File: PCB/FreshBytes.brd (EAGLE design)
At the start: 180.3 x 73.3 mm, 30 parts, among them T1 2N2222, T2 2N2222, T3 2N2222, T4 2N2222, X1 22-23-2021

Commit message: Add logo to BRD file, create gerbers, update BOM
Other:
- board size 180.3 x 73.3 mm -> 181 x 74 mm

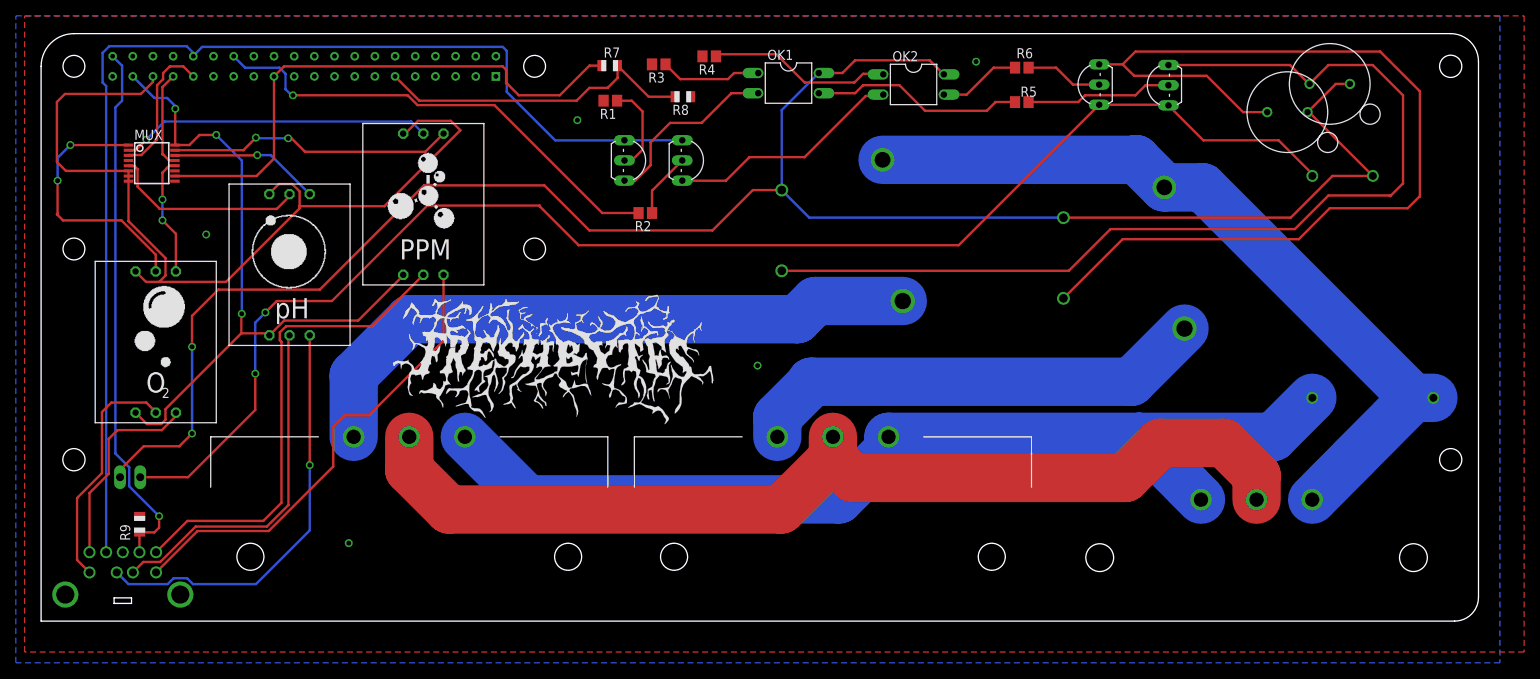
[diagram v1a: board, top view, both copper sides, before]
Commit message: Fix drill size for RPi headers. Swapping over to Rhino for CAD stuff
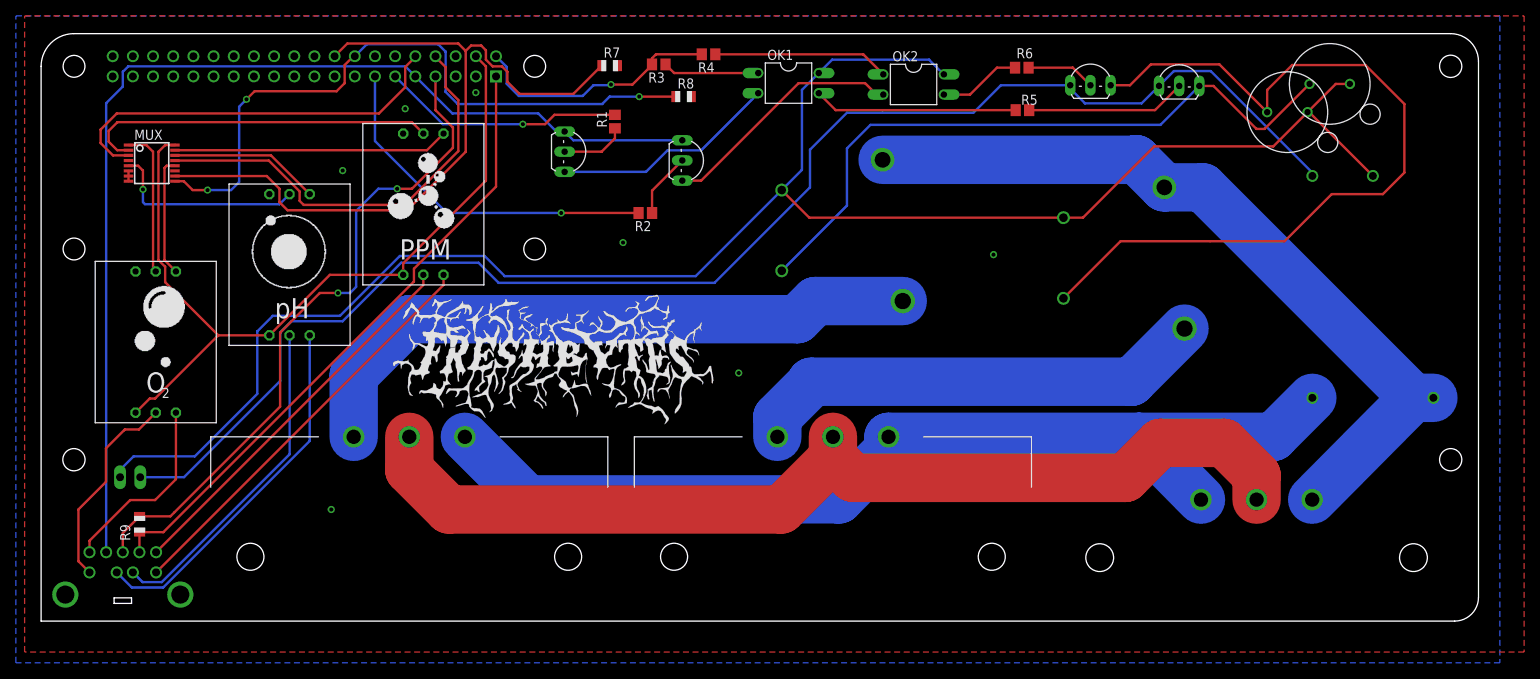
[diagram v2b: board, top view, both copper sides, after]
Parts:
- removed U$13: RPI_ZERO, FreshBytes:RPI_ZERO
- added U$10: RPI_ZERO, FreshBytes:RPI_ZERO
- moved T1 7.61 mm to (66.5, 59.1)
- moved T3 2.88 mm to (142.7, 68.6), turned to 0 degrees
- moved R1 2.69 mm to (71.6, 62.9), turned to 90 degrees
- moved T4 1.19 mm to (131.5, 68.7), turned to 0 degrees
- moved R5 1.02 mm to (122.9, 64.3)
- moved R4 0.27 mm to (83.4, 71.4)
- moved R8 0.09 mm to (80.3, 66.0), turned to 0 degrees
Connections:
- removed net 3.3V: U$13.3.3V
- removed net 3.3V1: U$13.3.3V1
- removed net 5V: U$13.5V
- removed net 5V1: U$13.5V1
- removed net N$30: MUX.GND, MUX.INH, MUX.VEE, U$13.GPIO19, U$5.GND, U$8.GND, U$9.GND
- removed net N$34: R7.2, R8.2, U$13.GPIO17
- new net 3.3V2: U$10.3.3V2
- new net GND5: U$10.GND5
- new net N$35: R1.2, U$10.GPIO17
- new net N$42: R9.1, U$10.GPIO4, U$4.P5
- new net N$43: MUX.B, R8.1, U$10.GPIO23
- new net N$44: R3.2, R4.2, U$10.5V
- net DGND: now also U$10.GND; no longer U$13.GPIO12
- net GND: now also MUX.GND, MUX.INH, MUX.VEE, R7.2, R8.2, U$10.GND2, U$10.GND3, U$10.GND4, U$10.GND7, U$10.GND8, U$5.GND, U$8.GND, U$9.GND; no longer MUX.B, R1.2, R3.2, R4.2, R8.1, R9.1, U$13.GND, U$13.GND1, U$13.GND2, U$13.GND3, U$13.GND4, U$13.GND5, U$13.GND6, U$13.GND7, U$4.P5
- net N$1: now also U$10.GPIO27; no longer U$13.ID_SC
- net N$21: now also U$10.RX; no longer U$13.GPIO6
- net N$29: now also U$10.GPIO24; no longer U$13.SCLK
- net N$33: now also U$10.5V2; no longer U$13.GPIO26
- net N$36: now also U$10.3.3V; no longer U$13.GPIO21
- net N$7: now also U$10.TX; no longer U$13.GPIO13
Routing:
- net N$30: track 111.6 -> 0.00 mm
- net N$42: track 0.00 -> 85.0 mm, vias 0 -> 2
- net N$43: track 0.00 -> 84.5 mm, vias 0 -> 3
- net N$7: track 12.3 -> 54.6 mm
- net N$18: track 127.0 -> 84.9 mm
- net N$34: track 40.9 -> 0.00 mm
- net N$21: track 17.8 -> 50.8 mm
- net N$44: track 0.00 -> 31.9 mm, vias 0 -> 1
- net N$35: track 0.00 -> 30.7 mm, vias 0 -> 1
- net N$29: track 69.6 -> 95.5 mm
- net N$16: track 127.3 -> 104.8 mm
- net N$1: track 60.3 -> 45.1 mm
- net N$33: track 87.0 -> 102.0 mm, vias 3 -> 0
- net N$26: track 33.5 -> 18.7 mm, vias 2 -> 0
- net N$36: track 67.7 -> 80.2 mm, vias 1 -> 0
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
